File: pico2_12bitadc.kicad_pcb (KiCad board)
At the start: 4 copper layers, 55.5 x 64.5 mm, 36 parts, among them J1 NOT_HDMI_A, J10 SMA90, J11 SMAEdge, J2 PCM1802, J3 AD9226 12bit ADC Board, J4 L R, J5 L, J6 HeadSw/Clipping, J7 R, J8 AudioJack2_Ground_Switch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

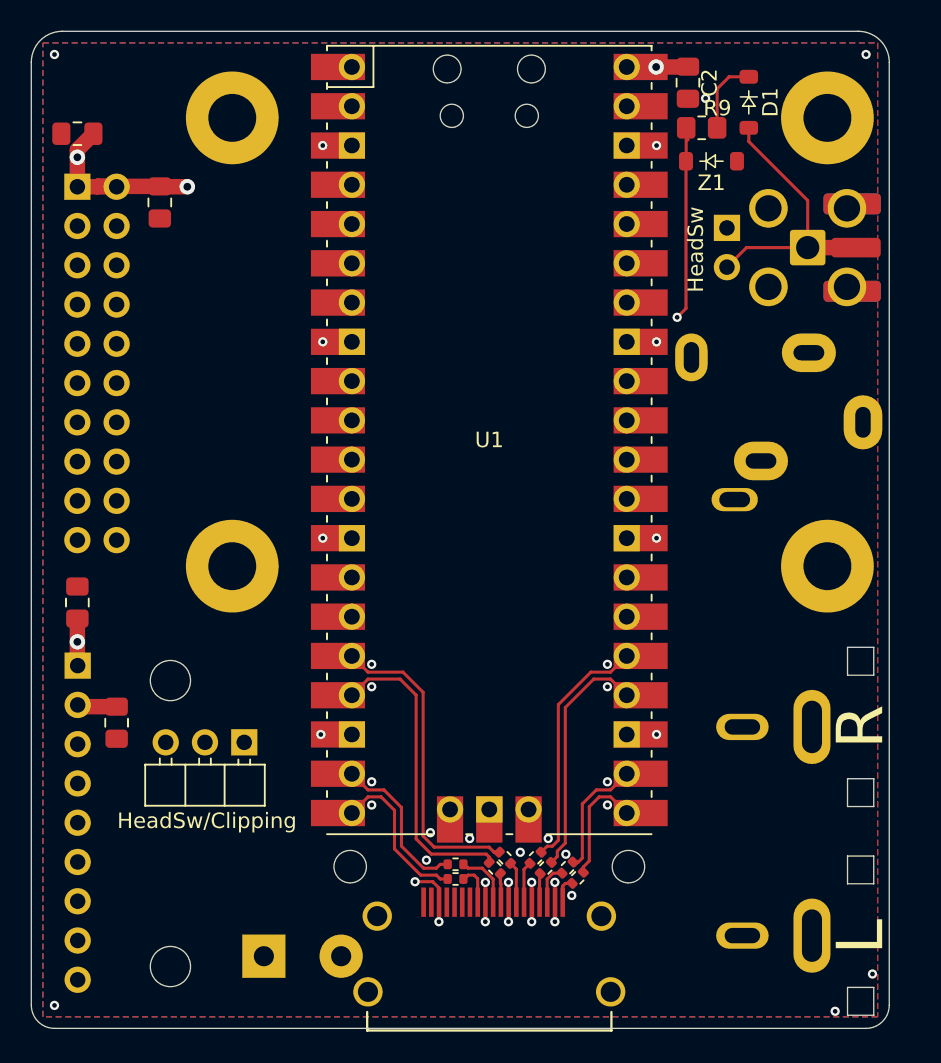
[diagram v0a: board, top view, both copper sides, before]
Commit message: Update pico2_12bitadc.kicad_pcb
Fixed hole spacing of the ad9226 pcb footprint
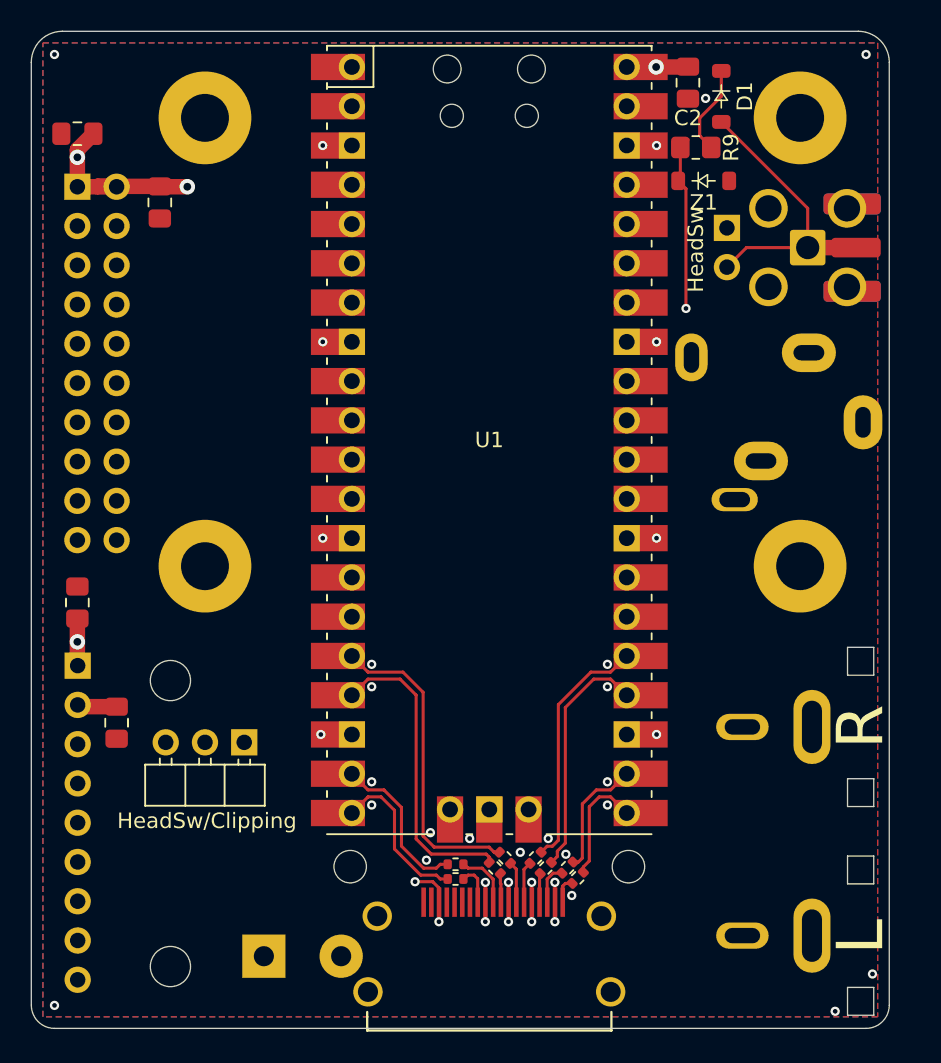
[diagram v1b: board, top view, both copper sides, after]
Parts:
- J2: value PCM1802 -> PCM1802 PCB
- J3: value AD9226 12bit ADC Board -> AD9226 PCB
- moved D1 1.82 mm to (135.6, 53.2)
- moved ? 1.77 mm to (102.2, 83.6)
- moved ? 1.77 mm to (102.2, 54.6)
- moved ? 1.76 mm to (140.7, 83.6)
- moved ? 1.76 mm to (140.7, 54.6)
- moved Z1 1.37 mm to (134.5, 58.7)
- moved R9 1.33 mm to (134.0, 56.5)
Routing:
- net Net-(D1-A): track 18.2 -> 19.3 mm
- net Net-(D2-K): track 56.4 -> 55.4 mm
- net Net-(D1-K): track 4.90 -> 5.84 mm

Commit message: Update pico2_12bitadc.kicad_pcb
Fixed trace near new hole position
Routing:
- net Net-(J3-Pin_5): track 89.4 -> 88.1 mm
- net Net-(J4-Pin_2): track 67.3 -> 67.9 mm
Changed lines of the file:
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@@
+	)
+	(segment
+		(start 97.917 53.34)
+		(end 97.917 62.738)
+		(width 0.2)
+		(layer "In1.Cu")
+		(net 34)
 	)
 	(segment
@@
 	)
 	(segment
-		(start 97.917 53.975)
-		(end 97.917 62.738)
-		(width 0.2)
-		(layer "In1.Cu")
-		(net 34)
-	)
-	(segment
 		(start 115.57 63.119)
 		(end 115.57 51.562)
@@
 	)
 	(segment
-		(start 101.981 49.911)
-		(end 97.917 53.975)
-		(width 0.2)
-		(layer "In1.Cu")
-		(net 34)
-	)
-	(segment
-		(start 101.981 49.911)
-		(end 100.8 51.092)
+		(start 101.346 49.911)
+		(end 97.917 53.34)
 		(width 0.2)
 		(layer "In1.Cu")
@@
 		(start 135.255 66.675)
 		(end 133.858 65.278)
+		(width 0.2)
+		(layer "In1.Cu")
+		(net 34)
+	)
+	(segment
+		(start 101.981 49.911)
+		(end 101.346 49.911)
 		(width 0.2)
 		(layer "In1.Cu")
@@
 	)
 	(segment
-		(start 137.922 82.169)
-		(end 141.301 78.79)
+		(start 137.16 90.3605)
+		(end 137.16 81.661)
+		(width 0.2)
+		(layer "In1.Cu")
+		(net 47)
+	)
+	(segment
+		(start 137 97.696)
+		(end 139.446 95.25)
+		(width 0.2)
+		(layer "In1.Cu")
+		(net 47)
+	)
+	(segment
+		(start 137 107.5)
+		(end 137 97.696)
+		(width 0.2)
+		(layer "In1.Cu")
+		(net 47)
+	)
+	(segment
+		(start 111.045 108.831)
+		(end 133.104 108.831)
+		(width 0.2)
+		(layer "In1.Cu")
+		(net 47)
+	)
+	(segment
+		(start 133.104 108.831)
+		(end 134.435 107.5)
+		(width 0.2)
+		(layer "In1.Cu")
+		(net 47)
+	)
+	(segment
+		(start 134.435 107.5)
+		(end 137 107.5)
+		(width 0.2)
+		(layer "In1.Cu")
+		(net 47)
+	)
+	(segment
+		(start 141.301 77.52)
+		(end 141.301 69.795)
+		(width 0.2)
+		(layer "In1.Cu")
+		(net 47)
+	)
+	(segment
+		(start 137.16 81.661)
+		(end 141.301 77.52)
+		(width 0.2)
+		(layer "In1.Cu")
+		(net 47)
+	)
+	(segment
+		(start 139.446 92.6465)
+		(end 137.16 90.3605)
 		(width 0.2)
 		(layer "In1.Cu")
@@
 		(width 0.2)
 		(layer "In1.Cu")
-		(net 47)
-	)
-	(segment
-		(start 141.301 78.79)
-		(end 141.301 69.795)
-		(width 0.2)
-		(layer "In1.Cu")
-		(net 47)
-	)
-	(segment
-		(start 137 107.5)
-		(end 137 97.696)
-		(width 0.2)
-		(layer "In1.Cu")
-		(net 47)
-	)
-	(segment
-		(start 137.922 91.1225)
-		(end 137.922 82.169)
-		(width 0.2)
-		(layer "In1.Cu")
-		(net 47)
-	)
-	(segment
-		(start 137 97.696)
-		(end 139.446 95.25)
-		(width 0.2)
-		(layer "In1.Cu")
-		(net 47)
-	)
-	(segment
-		(start 139.446 92.6465)
-		(end 137.922 91.1225)
-		(width 0.2)
-		(layer "In1.Cu")
-		(net 47)
-	)
-	(segment
-		(start 111.045 108.831)
-		(end 133.104 108.831)
-		(width 0.2)
-		(layer "In1.Cu")
-		(net 47)
-	)
-	(segment
-		(start 133.104 108.831)
-		(end 134.435 107.5)
-		(width 0.2)
-		(layer "In1.Cu")
-		(net 47)
-	)
-	(segment
-		(start 134.435 107.5)
-		(end 137 107.5)
-		(width 0.2)
-		(layer "In1.Cu")

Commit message: Update pico2_12bitadc.kicad_pcb
Added Name
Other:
- board text added: "Pico2-AD9226-PCM1802 PCB by Sev5000"
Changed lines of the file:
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@@
 		(layer "Edge.Cuts")
+	)
+	(gr_text "Pico2-AD9226-PCM1802 PCB\n         by Sev5000"
+		(at 135.89 111.76 90)
+		(layer "F.SilkS")
+		(effects
+			(font
+				(size 1 1)
+				(thickness 0.1)
+			)
+			(justify left bottom)
+		)
 	)
 	(segment

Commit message: Update pico2_12bitadc.kicad_pcb
Minor silkscreen adjustments
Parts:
- Pico 2: renamed from U1
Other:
- board text added: "Pico2 AD9226 PCM1802 Adapter by Sev5000"
- board text removed: "Pico2-AD9226-PCM1802 PCB by Sev5000"
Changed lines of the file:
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@@
 		(tags "SOD-123")
 		(property "Reference" "Z1"
-			(at 0 1.397 0)
+			(at 3.047 0 0)
 			(layer "F.SilkS")
 			(effects
@@
 		(tags "SOD-123")
 		(property "Reference" "D1"
-			(at 0.001 -1.524 90)
+			(at -0.126 -1.397 90)
 			(layer "F.SilkS")
 			(effects
@@
 		(descr "Through hole straight pin header, 2x20, 2.54mm pitch, double rows")
 		(tags "Through hole pin header THT 2x20 2.54mm double row")
-		(property "Reference" "U1"
+		(property "Reference" "Pico 2"
 			(at 0 0 0)
 			(layer "F.SilkS")
@@
 		(layer "Edge.Cuts")
 	)
-	(gr_text "Pico2-AD9226-PCM1802 PCB\n         by Sev5000"
-		(at 135.89 111.76 90)
+	(gr_text "Pico2 AD9226 PCM1802 Adapter\n\n         by Sev5000"
+		(at 137.668 112.141 90)
 		(layer "F.SilkS")
 		(effects

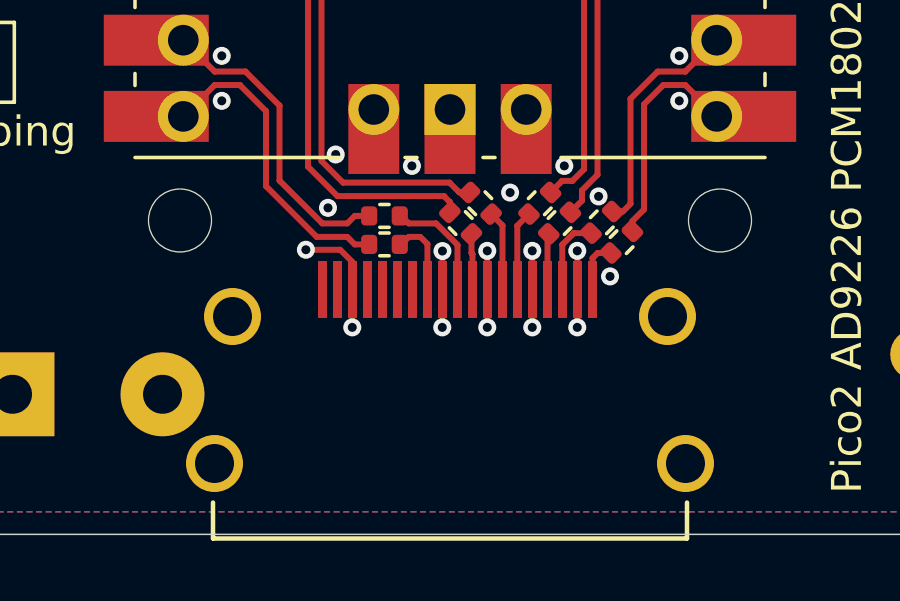
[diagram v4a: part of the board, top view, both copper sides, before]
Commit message: Update pico2_12bitadc.kicad_pcb
Increased pad length and through hole size of the hdmi connector for better compatability with other connector models
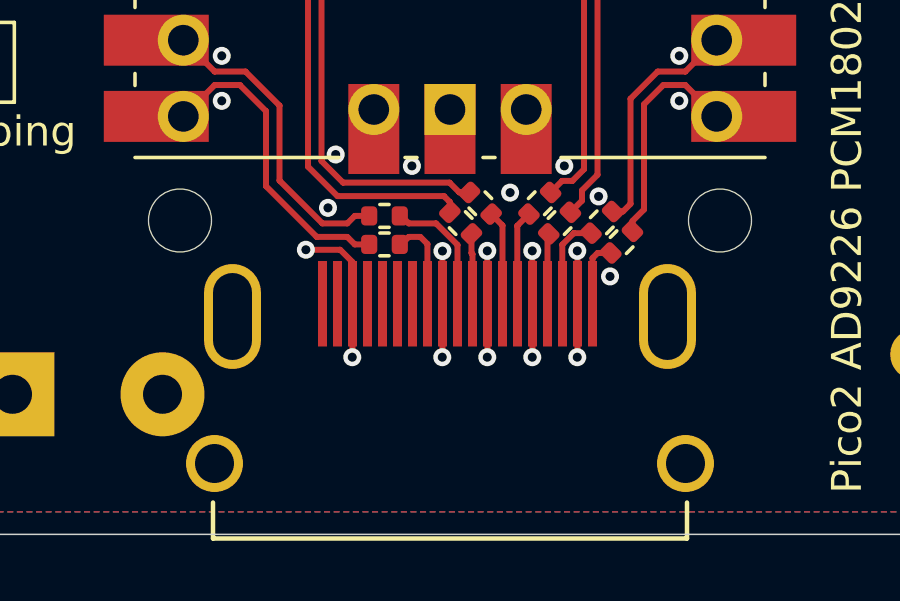
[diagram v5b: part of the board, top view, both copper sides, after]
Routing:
- net GND: track 14.1 -> 17.8 mm
- net Net-(J2-Pin_4): track 50.8 -> 49.6 mm
- net Net-(J2-Pin_9): track 48.6 -> 47.4 mm
- net Net-(J2-Pin_7): track 64.5 -> 65.6 mm
